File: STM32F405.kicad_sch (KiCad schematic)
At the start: 21 parts, among them SW1 SW_MEC_5G, U6 STM32F405RGTx, Y3 Crystal, Y4 Crystal

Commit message: fix logic
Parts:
- removed Y3: Crystal, Crystal:Crystal_SMD_3225-4Pin_3.2x2.5mm, symbol Device:Crystal
- added Y1: 25MHz, Crystal:Crystal_SMD_3225-4Pin_3.2x2.5mm, symbol Device:Crystal_GND24_Small
- C32, C35: value C_Small -> 18pF; footprint (none) -> Capacitor_SMD:C_0603_1608Metric
- C41, C42: value C_Small -> 20pF; footprint (none) -> Capacitor_SMD:C_0603_1608Metric
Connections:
- net GND1: now also Y1.2, Y1.4
- net at C32.1, U6.5 (PH0): now also Y1.1
- net at C35.1, U6.6 (PH1): now also Y1.3
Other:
- moved on the sheet: C32, C35
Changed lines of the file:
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@@
 (kicad_sch (version 20230121) (generator eeschema)
   (paper "A4")
+  (junction (at 82.55 66.04) (diameter 0) (color 0 0 0 0)
+  )
   (junction (at 152.4 142.24) (diameter 0) (color 0 0 0 0)
   )
   (junction (at 113.03 30.48) (diameter 0) (color 0 0 0 0)
+  )
+  (junction (at 73.66 73.66) (diameter 0) (color 0 0 0 0)
   )
   (junction (at 243.84 29.21) (diameter 0) (color 0 0 0 0)
@@
     (stroke (width 0) (type default))
   )
+  (wire (pts (xy 82.55 66.04) (xy 82.55 73.66))
+    (stroke (width 0) (type default))
+  )
+  (wire (pts (xy 63.5 63.5) (xy 66.04 63.5))
+    (stroke (width 0) (type default))
+  )
   (wire (pts (xy 243.84 60.96) (xy 243.84 64.77))
     (stroke (width 0) (type default))
@@
     (stroke (width 0) (type default))
   )
-  (wire (pts (xy 73.66 63.5) (xy 73.66 66.04))
+  (wire (pts (xy 73.66 63.5) (xy 73.66 67.31))
     (stroke (width 0) (type default))
   )
@@
     (stroke (width 0) (type default))
   )
-  (wire (pts (xy 73.66 63.5) (xy 72.39 63.5))
-    (stroke (width 0) (type default))
-  )
   (wire (pts (xy 36.83 54.61) (xy 36.83 57.15))
     (stroke (width 0) (type default))
@@
     (stroke (width 0) (type default))
   )
-  (wire (pts (xy 63.5 71.12) (xy 63.5 73.66))
+  (wire (pts (xy 63.5 72.39) (xy 63.5 73.66))
     (stroke (width 0) (type default))
   )
@@
     (stroke (width 0) (type default))
   )
+  (wire (pts (xy 68.58 66.04) (xy 82.55 66.04))
+    (stroke (width 0) (type default))
+  )
   (wire (pts (xy 266.7 39.37) (xy 278.13 39.37))
     (stroke (width 0) (type default))
@@
     (stroke (width 0) (type default))
   )
-  (wire (pts (xy 63.5 63.5) (xy 64.77 63.5))
-    (stroke (width 0) (type default))
-  )
   (wire (pts (xy 243.84 39.37) (xy 255.27 39.37))
     (stroke (width 0) (type default))
@@
     (stroke (width 0) (type default))
   )
-  (wire (pts (xy 73.66 71.12) (xy 73.66 73.66))
+  (wire (pts (xy 82.55 60.96) (xy 82.55 66.04))
+    (stroke (width 0) (type default))
+  )
+  (wire (pts (xy 73.66 72.39) (xy 73.66 73.66))
     (stroke (width 0) (type default))
   )
@@
     (stroke (width 0) (type default))
   )
+  (wire (pts (xy 71.12 63.5) (xy 73.66 63.5))
+    (stroke (width 0) (type default))
+  )
   (wire (pts (xy 130.81 95.25) (xy 134.62 95.25))
     (stroke (width 0) (type default))
@@
     (stroke (width 0) (type default))
   )
-  (wire (pts (xy 63.5 63.5) (xy 63.5 66.04))
+  (wire (pts (xy 63.5 63.5) (xy 63.5 67.31))
     (stroke (width 0) (type default))
   )
@@
     (stroke (width 0) (type default))
   )
+  (wire (pts (xy 73.66 73.66) (xy 82.55 73.66))
+    (stroke (width 0) (type default))
+  )
   (wire (pts (xy 231.14 40.64) (xy 231.14 36.83))
     (stroke (width 0) (type default))
@@
   )
   (wire (pts (xy 58.42 49.53) (xy 95.25 49.53))
+    (stroke (width 0) (type default))
+  )
+  (wire (pts (xy 68.58 60.96) (xy 82.55 60.96))
     (stroke (width 0) (type default))
   )
@@
     )
   )
-  (symbol (lib_id "Device:C_Small") (at 63.5 68.58 0) (unit 1)
-    (in_bom yes) (on_board yes) (dnp no)
-    (property "Reference" "C32" (at 60.96 67.3163 0)
-      (effects (font (size 1.27 1.27)) (justify right))
-    )
-    (property "Value" "C_Small" (at 62.23 71.12 0)
-      (effects (font (size 1.27 1.27)) (justify right))
-    )
-    (property "Footprint" "" (at 63.5 68.58 0)
-      (effects (font (size 1.27 1.27)) hide)
-    )
-    (property "Datasheet" "~" (at 63.5 68.58 0)
+  (symbol (lib_id "Device:C_Small") (at 63.5 69.85 0) (unit 1)
+    (in_bom yes) (on_board yes) (dnp no)
+    (property "Reference" "C32" (at 60.96 68.5863 0)
+      (effects (font (size 1.27 1.27)) (justify right))
+    )
+    (property "Value" "18pF" (at 62.23 72.39 0)
+      (effects (font (size 1.27 1.27)) (justify right))
+    )
+    (property "Footprint" "Capacitor_SMD:C_0603_1608Metric" (at 63.5 69.85 0)
+      (effects (font (size 1.27 1.27)) hide)
+    )
+    (property "Datasheet" "~" (at 63.5 69.85 0)
       (effects (font (size 1.27 1.27)) hide)
     )
@@
     )
   )
+  (symbol (lib_id "Device:Crystal_GND24_Small") (at 68.58 63.5 0) (unit 1)
+    (in_bom yes) (on_board yes) (dnp no)
+    (property "Reference" "Y1" (at 68.58 55.88 0)
+      (effects (font (size 1.27 1.27)))
+    )
+    (property "Value" "25MHz" (at 68.58 58.42 0)
+      (effects (font (size 1.27 1.27)))
+    )
+    (property "Footprint" "Crystal:Crystal_SMD_3225-4Pin_3.2x2.5mm" (at 68.58 63.5 0)
+      (effects (font (size 1.27 1.27)) hide)
+    )
+    (property "Datasheet" "~" (at 68.58 63.5 0)
+      (effects (font (size 1.27 1.27)) hide)
+    )
+    (pin "2")
+    (pin "4")
+    (pin "1")
+    (pin "3")
+    (instances
+      (project "schematic_MD"
+        (path "/3152684b-d11f-4a9a-8e6c-09965044adbd/878f32b7-0d3d-4f49-a9dc-ebc0f2e1c793"
+          (reference "Y1") (unit 1)
+        )
+      )
+    )
+  )
   (symbol (lib_id "power:GND1") (at 115.57 135.89 0) (unit 1)
     (in_bom yes) (on_board yes) (dnp no) (fields_autoplaced)
@@
       (effects (font (size 1.27 1.27)) (justify right))
     )
-    (property "Value" "C_Small" (at 143.51 139.7 0)
-      (effects (font (size 1.27 1.27)) (justify right))
-    )
-    (property "Footprint" "" (at 142.24 137.16 0)
+    (property "Value" "20pF" (at 143.51 139.7 0)
+      (effects (font (size 1.27 1.27)) (justify right))
+    )
+    (property "Footprint" "Capacitor_SMD:C_0603_1608Metric" (at 142.24 137.16 0)
       (effects (font (size 1.27 1.27)) hide)
     )
@@
     )
   )
-  (symbol (lib_id "Device:C_Small") (at 73.66 68.58 0) (unit 1)
-    (in_bom yes) (on_board yes) (dnp no)
-    (property "Reference" "C35" (at 71.12 67.3163 0)
-      (effects (font (size 1.27 1.27)) (justify right))
-    )
-    (property "Value" "C_Small" (at 72.39 71.12 0)
-      (effects (font (size 1.27 1.27)) (justify right))
-    )
-    (property "Footprint" "" (at 73.66 68.58 0)
-      (effects (font (size 1.27 1.27)) hide)
-    )
-    (property "Datasheet" "~" (at 73.66 68.58 0)
+  (symbol (lib_id "Device:C_Small") (at 73.66 69.85 0) (unit 1)
+    (in_bom yes) (on_board yes) (dnp no)
+    (property "Reference" "C35" (at 71.12 68.5863 0)
+      (effects (font (size 1.27 1.27)) (justify right))
+    )
+    (property "Value" "18pF" (at 72.39 72.39 0)
+      (effects (font (size 1.27 1.27)) (justify right))
+    )
+    (property "Footprint" "Capacitor_SMD:C_0603_1608Metric" (at 73.66 69.85 0)
+      (effects (font (size 1.27 1.27)) hide)
+    )
+    (property "Datasheet" "~" (at 73.66 69.85 0)
       (effects (font (size 1.27 1.27)) hide)
     )
@@
       (effects (font (size 1.27 1.27)) (justify right))
     )
-    (property "Value" "C_Small" (at 153.67 139.7 0)
-      (effects (font (size 1.27 1.27)) (justify right))
-    )
-    (property "Footprint" "" (at 152.4 137.16 0)
+    (property "Value" "20pF" (at 153.67 139.7 0)
+      (effects (font (size 1.27 1.27)) (justify right))
+    )
+    (property "Footprint" "Capacitor_SMD:C_0603_1608Metric" (at 152.4 137.16 0)
       (effects (font (size 1.27 1.27)) hide)
     )
@@
         )
       )
-    )
-  )
-  (symbol (lib_id "Device:Crystal") (at 68.58 63.5 0) (unit 1)
-    (in_bom yes) (on_board yes) (dnp no) (fields_autoplaced)
-    (property "Reference" "Y3" (at 68.58 55.88 0)
-      (effects (font (size 1.27 1.27)))
-    )
-    (property "Value" "Crystal" (at 68.58 58.42 0)
-      (effects (font (size 1.27 1.27)))
-    )
-    (property "Footprint" "Crystal:Crystal_SMD_3225-4Pin_3.2x2.5mm" (at 68.58 63.5 0)
-      (effects (font (size 1.27 1.27)) hide)
-    )
-    (property "Datasheet" "~" (at 68.58 63.5 0)
-      (effects (font (size 1.27 1.27)) hide)
-    )
-    (pin "2")
-    (pin "1")
-    (instances
-      (project "schematic_MD"
-        (path "/3152684b-d11f-4a9a-8e6c-09965044adbd/878f32b7-0d3d-4f49-a9dc-ebc0f2e1c793"
-          (reference "Y3") (unit 1)
-        )
-      )

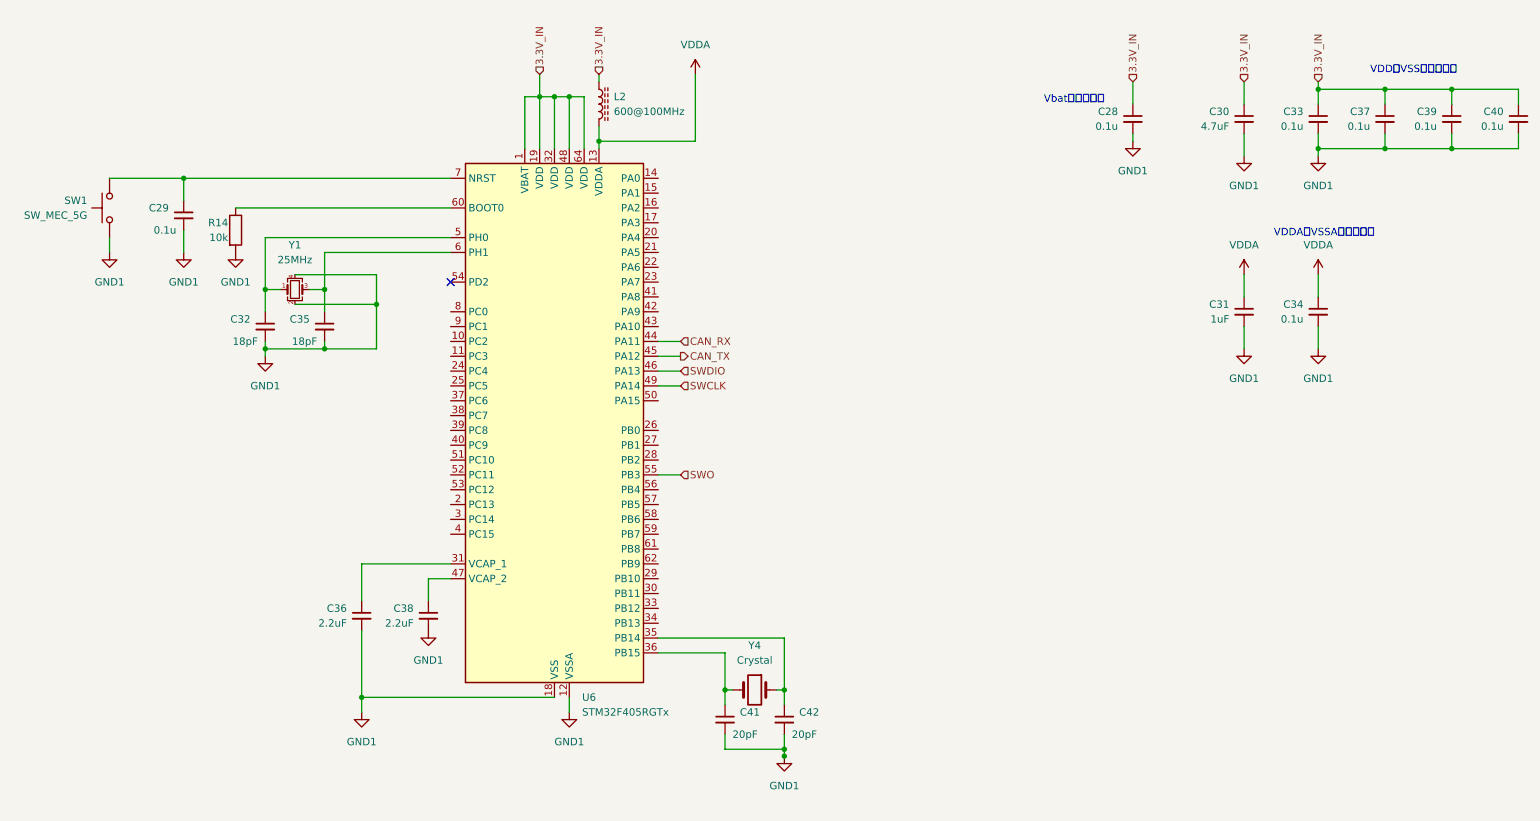
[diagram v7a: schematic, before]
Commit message: logic design update
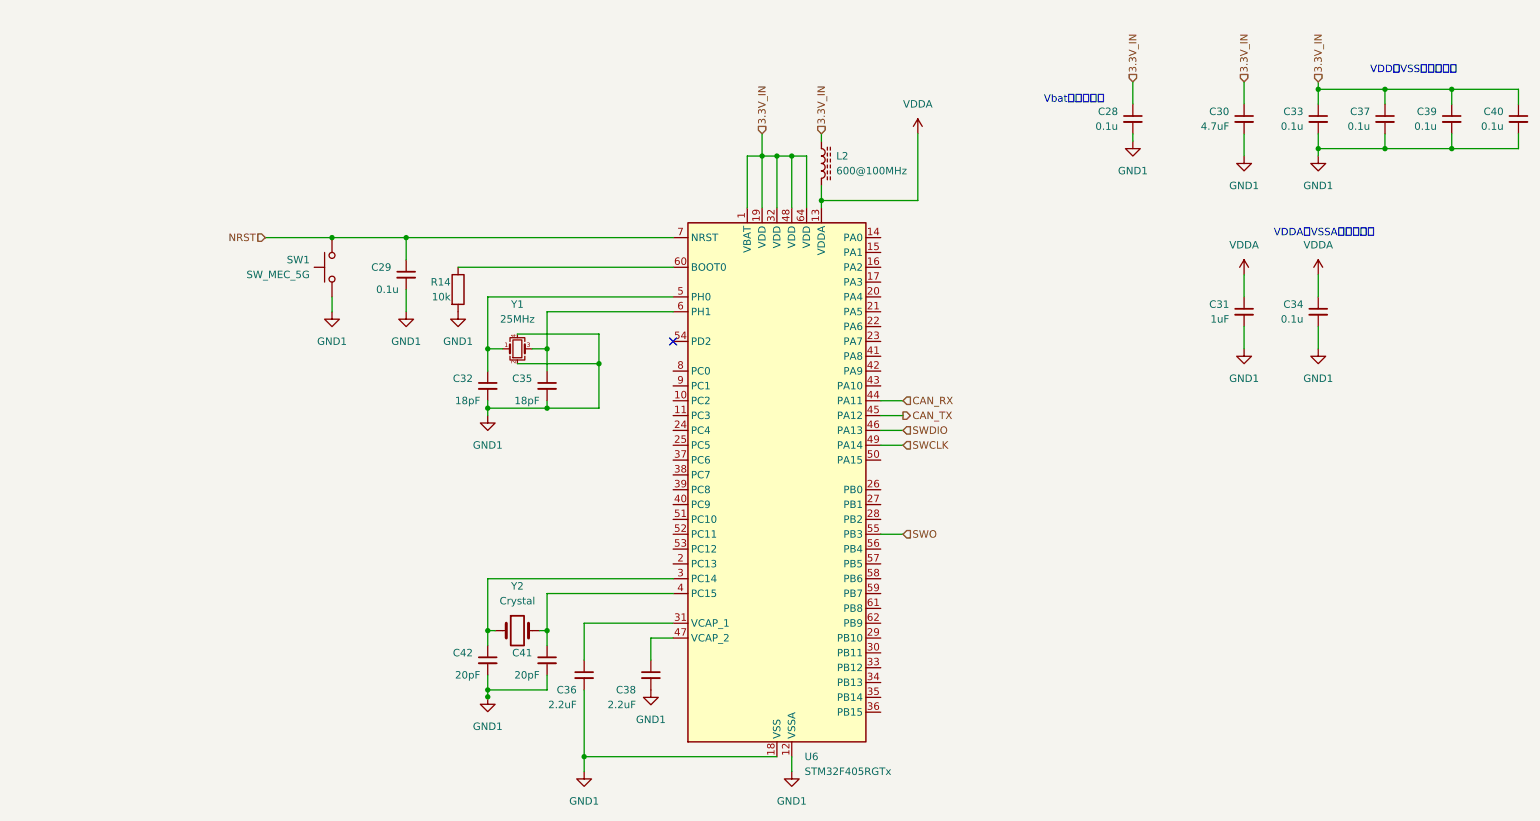
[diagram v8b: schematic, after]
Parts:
- removed Y4: Crystal, Crystal:Crystal_SMD_3215-2Pin_3.2x1.5mm, symbol Device:Crystal
- added Y2: Crystal, Crystal:Crystal_SMD_3215-2Pin_3.2x1.5mm, symbol Device:Crystal
- C32, C35, C41, C42: footprint Capacitor_SMD:C_0603_1608Metric -> Capacitor_SMD:C_0402_1005Metric
- SW1: footprint Button_Switch_THT:SW_PUSH_6mm -> Button_Switch_SMD:SW_Push_1P1T_XKB_TS-1187A
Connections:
- net at C42.1: now also U6.3 (PC14), Y2.1; no longer U6.35 (PB14)
- net at C41.1: now also U6.4 (PC15), Y2.2; no longer U6.36 (PB15)
- net NRST: now reaches C29.1, SW1.4 (B), U6.7 (NRST)
- net NRST: now also SW1.2 (B); no longer SW1.3 (B)
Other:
- moved on the sheet: C29, C32, C35, C36, C38, L2, R14, SW1, U6, Y1
